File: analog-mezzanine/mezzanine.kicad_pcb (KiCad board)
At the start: 2 copper layers, 90 x 90 mm, 4 parts

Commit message: start layout
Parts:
- added C1: 200n, Capacitor_SMD:C_1206_3216Metric, F.Cu at (149.5, 162.3)
- added C10: 10n, Capacitor_SMD:C_0805_2012Metric, F.Cu at (143.7, 173.0)
- added C11: 10n, Capacitor_SMD:C_0805_2012Metric, F.Cu at (140.7, 173.0)
- added C12: low ESR 2.2u, Capacitor_SMD:C_1206_3216Metric, F.Cu at (132.8, 162.3)
- added C13: 10u alum poly, Capacitor_THT:CP_Radial_D8.0mm_P3.50mm, F.Cu at (127.3, 153.0)
- added C14: 0.1u, Capacitor_SMD:C_1206_3216Metric, F.Cu at (129.4, 162.3)
- added C15: 10u alum poly, Capacitor_THT:CP_Radial_D8.0mm_P3.50mm, F.Cu at (117.8, 153.0)
- added C16: 0.1u, Capacitor_SMD:C_1206_3216Metric, F.Cu at (126.1, 162.3)
- added C17: 0.01u, Capacitor_SMD:C_1206_3216Metric, B.Cu at (38.3, 76.4)
- added C18: 200n, Capacitor_SMD:C_1206_3216Metric, F.Cu at (195.7, 160.3)
- added C19: 200n, Capacitor_SMD:C_1206_3216Metric, F.Cu at (192.4, 160.3)
- added C2: 200n, Capacitor_SMD:C_1206_3216Metric, F.Cu at (146.2, 162.3)
- added C20: 10u alum poly, Capacitor_THT:CP_Radial_D8.0mm_P3.50mm, F.Cu at (192.6, 151.0)
- added C21: 10u alum poly, Capacitor_THT:CP_Radial_D8.0mm_P3.50mm, F.Cu at (183.1, 151.0)
- added C22: low ESR 2.2u, Capacitor_SMD:C_1206_3216Metric, F.Cu at (189.0, 160.3)
- added C23: 10n, Capacitor_SMD:C_0805_2012Metric, F.Cu at (195.9, 171.0)
- added C24: 10n, Capacitor_SMD:C_0805_2012Metric, F.Cu at (192.9, 171.0)
- added C25: low ESR 2.2u, Capacitor_SMD:C_1206_3216Metric, F.Cu at (185.7, 160.3)
- added C26: low ESR 2.2u, Capacitor_SMD:C_1206_3216Metric, F.Cu at (182.3, 160.3)
- added C27: 10n, Capacitor_SMD:C_0805_2012Metric, F.Cu at (189.9, 171.0)
- added C28: 10n, Capacitor_SMD:C_0805_2012Metric, F.Cu at (186.9, 171.0)
- added C29: low ESR 2.2u, Capacitor_SMD:C_1206_3216Metric, F.Cu at (179.0, 160.3)
- added C3: 10u alum poly, Capacitor_THT:CP_Radial_D8.0mm_P3.50mm, F.Cu at (146.4, 153.0)
- added C30: 10u alum poly, Capacitor_THT:CP_Radial_D8.0mm_P3.50mm, F.Cu at (173.5, 151.0)
- added C31: 0.1u, Capacitor_SMD:C_1206_3216Metric, F.Cu at (175.6, 160.3)
- added C32: 10u alum poly, Capacitor_THT:CP_Radial_D8.0mm_P3.50mm, F.Cu at (164.0, 151.0)
- added C33: 0.1u, Capacitor_SMD:C_1206_3216Metric, F.Cu at (172.3, 160.3)
- added C34: 0.01u, Capacitor_SMD:C_1206_3216Metric, B.Cu at (38.3, 84.8)
- added C35: 200n, Capacitor_SMD:C_1206_3216Metric, F.Cu at (131.7, 105.0)
- added C36: 200n, Capacitor_SMD:C_1206_3216Metric, F.Cu at (131.7, 108.3)
- added C37: 10u alum poly, Capacitor_THT:CP_Radial_D8.0mm_P3.50mm, F.Cu at (122.3, 108.1)
- added C38: 10u alum poly, Capacitor_THT:CP_Radial_D8.0mm_P3.50mm, F.Cu at (122.3, 117.6)
- added C39: low ESR 2.2u, Capacitor_SMD:C_1206_3216Metric, F.Cu at (131.7, 111.7)
- added C4: 10u alum poly, Capacitor_THT:CP_Radial_D8.0mm_P3.50mm, F.Cu at (136.9, 153.0)
- added C40: 10n, Capacitor_SMD:C_0805_2012Metric, F.Cu at (142.3, 104.8)
- added C41: 10n, Capacitor_SMD:C_0805_2012Metric, F.Cu at (142.3, 107.8)
- added C42: low ESR 2.2u, Capacitor_SMD:C_1206_3216Metric, F.Cu at (131.7, 115.0)
- added C43: low ESR 2.2u, Capacitor_SMD:C_1206_3216Metric, F.Cu at (131.7, 118.4)
- added C44: 10n, Capacitor_SMD:C_0805_2012Metric, F.Cu at (142.3, 110.8)
- added C45: 10n, Capacitor_SMD:C_0805_2012Metric, F.Cu at (142.3, 113.8)
- added C46: low ESR 2.2u, Capacitor_SMD:C_1206_3216Metric, F.Cu at (131.7, 121.7)
- added C47: 10u alum poly, Capacitor_THT:CP_Radial_D8.0mm_P3.50mm, F.Cu at (122.3, 127.2)
- added C48: 0.1u, Capacitor_SMD:C_1206_3216Metric, F.Cu at (131.7, 125.1)
- added C49: 10u alum poly, Capacitor_THT:CP_Radial_D8.0mm_P3.50mm, F.Cu at (122.3, 136.7)
- added C5: low ESR 2.2u, Capacitor_SMD:C_1206_3216Metric, F.Cu at (142.8, 162.3)
- added C50: 0.1u, Capacitor_SMD:C_1206_3216Metric, F.Cu at (131.7, 128.4)
- added C51: 0.01u, Capacitor_SMD:C_1206_3216Metric, B.Cu at (38.3, 93.2)
- added C52: 200n, Capacitor_SMD:C_1206_3216Metric, F.Cu at (267.5, 159.7)
- added C53: 200n, Capacitor_SMD:C_1206_3216Metric, F.Cu at (264.2, 159.7)
- added C54: 10u alum poly, Capacitor_THT:CP_Radial_D8.0mm_P3.50mm, F.Cu at (264.4, 150.3)
- added C55: 10u alum poly, Capacitor_THT:CP_Radial_D8.0mm_P3.50mm, F.Cu at (254.9, 150.3)
- added C56: low ESR 2.2u, Capacitor_SMD:C_1206_3216Metric, F.Cu at (260.8, 159.7)
- added C57: 10n, Capacitor_SMD:C_0805_2012Metric, F.Cu at (267.7, 170.3)
- added C58: 10n, Capacitor_SMD:C_0805_2012Metric, F.Cu at (264.7, 170.3)
- added C59: low ESR 2.2u, Capacitor_SMD:C_1206_3216Metric, F.Cu at (257.5, 159.7)
- added C6: 10n, Capacitor_SMD:C_0805_2012Metric, F.Cu at (149.7, 173.0)
- added C60: low ESR 2.2u, Capacitor_SMD:C_1206_3216Metric, F.Cu at (254.1, 159.7)
- added C61: 10n, Capacitor_SMD:C_0805_2012Metric, F.Cu at (261.7, 170.3)
- added C62: 10n, Capacitor_SMD:C_0805_2012Metric, F.Cu at (258.7, 170.3)
- added C63: low ESR 2.2u, Capacitor_SMD:C_1206_3216Metric, F.Cu at (250.8, 159.7)
- added C64: 10u alum poly, Capacitor_THT:CP_Radial_D8.0mm_P3.50mm, F.Cu at (245.3, 150.3)
- added C65: 0.1u, Capacitor_SMD:C_1206_3216Metric, F.Cu at (247.4, 159.7)
- added C66: 10u alum poly, Capacitor_THT:CP_Radial_D8.0mm_P3.50mm, F.Cu at (235.8, 150.3)
- added C67: 0.1u, Capacitor_SMD:C_1206_3216Metric, F.Cu at (244.1, 159.7)
- added C68: 0.01u, Capacitor_SMD:C_1206_3216Metric, B.Cu at (38.3, 101.4)
- added C7: 10n, Capacitor_SMD:C_0805_2012Metric, F.Cu at (146.7, 173.0)
- added C8: low ESR 2.2u, Capacitor_SMD:C_1206_3216Metric, F.Cu at (139.5, 162.3)
- added C9: low ESR 2.2u, Capacitor_SMD:C_1206_3216Metric, F.Cu at (136.1, 162.3)
- added FL1: Filter_EMI_LLL, Library:WE-SL3_744252XXX, B.Cu at (57.4, 50.0)
- added FL2: Filter_EMI_LLL, Library:WE-SL3_744252XXX, B.Cu at (71.1, 50.0)
- added FL3: Filter_EMI_LLL, Library:WE-SL3_744252XXX, F.Cu at (58.8, 50.0)
- added FL4: Filter_EMI_LLL, Library:WE-SL3_744252XXX, F.Cu at (69.7, 50.0)
- added J1: Conn_Coaxial, Connector_Coaxial:MMCX_Molex_73415-0961_Horizontal_1.0mm-PCB, F.Cu at (25.1, 76.4)
- added J2: Conn_Coaxial, Connector_Coaxial:MMCX_Molex_73415-0961_Horizontal_1.0mm-PCB, F.Cu at (25.1, 84.9)
- added J3: Conn_Coaxial, Connector_Coaxial:MMCX_Molex_73415-0961_Horizontal_1.0mm-PCB, F.Cu at (25.1, 93.2)
- added J4: Conn_Coaxial, Connector_Coaxial:MMCX_Molex_73415-0961_Horizontal_1.0mm-PCB, F.Cu at (25.1, 101.4)
- added J5: Conn_Coaxial, Connector_Coaxial:MMCX_Molex_73415-1471_Vertical, F.Cu at (46.6, 74.1)
- added J6: Conn_Coaxial, Connector_Coaxial:MMCX_Molex_73415-1471_Vertical, F.Cu at (46.6, 82.5)
- added J7: Conn_Coaxial, Connector_Coaxial:MMCX_Molex_73415-1471_Vertical, F.Cu at (46.6, 90.8)
- added J8: Conn_Coaxial, Connector_Coaxial:MMCX_Molex_73415-1471_Vertical, F.Cu at (46.6, 99.1)
- added J9: LD15P24A4GV00LF, Library:AMPHENOL_LD15P24A4GV00LF, F.Cu at (64.2, 38.4)
- added JP1: SolderJumper_2_Open, Jumper:SolderJumper-2_P1.3mm_Open_RoundedPad1.0x1.5mm, B.Cu at (85.0, 38.4)
- added JP2: SolderJumper_2_Open, Jumper:SolderJumper-2_P1.3mm_Open_RoundedPad1.0x1.5mm, B.Cu at (47.6, 42.4)
- added JP3: SolderJumper_2_Open, Jumper:SolderJumper-2_P1.3mm_Open_RoundedPad1.0x1.5mm, B.Cu at (65.6, 34.5)
- added JP4: SolderJumper_2_Open, Jumper:SolderJumper-2_P1.3mm_Open_RoundedPad1.0x1.5mm, B.Cu at (62.9, 34.5)
- added JP5: SolderJumper_2_Open, Jumper:SolderJumper-2_P1.3mm_Open_RoundedPad1.0x1.5mm, B.Cu at (64.2, 42.4)
- added L1: 33u, Library:IND_VLS4015CX-330M-H, F.Cu at (135.2, 168.4)
- added L2: 33u, Library:IND_VLS4015CX-330M-H, F.Cu at (129.6, 168.4)
- added L3: 33u, Library:IND_VLS4015CX-330M-H, F.Cu at (181.4, 166.4)
- added L4: 33u, Library:IND_VLS4015CX-330M-H, F.Cu at (175.9, 166.4)
- added L5: 33u, Library:IND_VLS4015CX-330M-H, F.Cu at (137.8, 119.3)
- added L6: 33u, Library:IND_VLS4015CX-330M-H, F.Cu at (137.8, 124.9)
- added L7: 33u, Library:IND_VLS4015CX-330M-H, F.Cu at (253.2, 165.8)
- added L8: 33u, Library:IND_VLS4015CX-330M-H, F.Cu at (247.7, 165.8)
- added R1: 1k, Resistor_SMD:R_0805_2012Metric, F.Cu at (34.7, 76.4)
- added R10: 2k, Resistor_SMD:R_0805_2012Metric, F.Cu at (36.5, 86.8)
- added R11: 324k, Resistor_SMD:R_1206_3216Metric, F.Cu at (189.1, 165.9)
- added R12: 100k, Resistor_SMD:R_1206_3216Metric, F.Cu at (185.8, 165.9)
- added R13: 1k, Resistor_SMD:R_0805_2012Metric, F.Cu at (34.7, 93.2)
- added R14: 324k, Resistor_SMD:R_1206_3216Metric, F.Cu at (137.3, 105.0)
- added R15: 100k, Resistor_SMD:R_1206_3216Metric, F.Cu at (137.3, 108.3)
- added R16: 2k, Resistor_SMD:R_0805_2012Metric, F.Cu at (36.5, 95.2)
- added R17: 324k, Resistor_SMD:R_1206_3216Metric, F.Cu at (137.3, 111.6)
- added R18: 100k, Resistor_SMD:R_1206_3216Metric, F.Cu at (137.3, 114.9)
- added R19: 1k, Resistor_SMD:R_0805_2012Metric, F.Cu at (34.7, 101.4)
- added R2: 324k, Resistor_SMD:R_1206_3216Metric, F.Cu at (149.5, 167.9)
- added R20: 324k, Resistor_SMD:R_1206_3216Metric, F.Cu at (267.6, 165.3)
- added R21: 100k, Resistor_SMD:R_1206_3216Metric, F.Cu at (264.3, 165.3)
- added R22: 2k, Resistor_SMD:R_0805_2012Metric, F.Cu at (36.5, 103.4)
- added R23: 324k, Resistor_SMD:R_1206_3216Metric, F.Cu at (260.9, 165.3)
- added R24: 100k, Resistor_SMD:R_1206_3216Metric, F.Cu at (257.6, 165.3)
- added R3: 100k, Resistor_SMD:R_1206_3216Metric, F.Cu at (146.2, 167.9)
- added R4: 2k, Resistor_SMD:R_0805_2012Metric, F.Cu at (36.5, 78.4)
- added R5: 324k, Resistor_SMD:R_1206_3216Metric, F.Cu at (142.9, 167.9)
- added R6: 100k, Resistor_SMD:R_1206_3216Metric, F.Cu at (139.6, 167.9)
- added R7: 1k, Resistor_SMD:R_0805_2012Metric, F.Cu at (34.7, 84.8)
- added R8: 324k, Resistor_SMD:R_1206_3216Metric, F.Cu at (195.8, 165.9)
- added R9: 100k, Resistor_SMD:R_1206_3216Metric, F.Cu at (192.5, 165.9)
- added Rt1: 50, Resistor_SMD:R_0805_2012Metric, F.Cu at (31.2, 75.5)
- added Rt2: 50, Resistor_SMD:R_0805_2012Metric, F.Cu at (42.4, 74.1)
- added Rt3: 50, Resistor_SMD:R_0805_2012Metric, F.Cu at (31.2, 83.9)
- added Rt4: 50, Resistor_SMD:R_0805_2012Metric, F.Cu at (42.4, 82.6)
- added Rt5: 50, Resistor_SMD:R_0805_2012Metric, F.Cu at (31.2, 92.3)
- added Rt6: 50, Resistor_SMD:R_0805_2012Metric, F.Cu at (42.4, 90.9)
- added Rt7: 50, Resistor_SMD:R_0805_2012Metric, F.Cu at (31.2, 100.5)
- added Rt8: 50, Resistor_SMD:R_0805_2012Metric, F.Cu at (42.4, 99.1)
- added U1: minus TPS7A3001MDGNTEP, Library:DGN8_1P89X1P57, F.Cu at (117.5, 163.2)
- added U10: minus TPS7A3001MDGNTEP, Library:DGN8_1P89X1P57, F.Cu at (235.5, 160.5)
- added U11: plus TPS7A4901DGNT, Library:SOP65P490X110-9N, F.Cu at (240.1, 161.1)
- added U12: BUF602xDBV, Package_TO_SOT_SMD:SOT-23-5, F.Cu at (38.8, 100.3)
- added U2: plus TPS7A4901DGNT, Library:SOP65P490X110-9N, F.Cu at (122.1, 163.8)
- added U3: BUF602xDBV, Package_TO_SOT_SMD:SOT-23-5, F.Cu at (38.8, 75.3)
- added U4: minus TPS7A3001MDGNTEP, Library:DGN8_1P89X1P57, F.Cu at (163.7, 161.2)
- added U5: plus TPS7A4901DGNT, Library:SOP65P490X110-9N, F.Cu at (168.3, 161.8)
- added U6: BUF602xDBV, Package_TO_SOT_SMD:SOT-23-5, F.Cu at (38.8, 83.7)
- added U7: minus TPS7A3001MDGNTEP, Library:DGN8_1P89X1P57, F.Cu at (132.6, 137.0)
- added U8: plus TPS7A4901DGNT, Library:SOP65P490X110-9N, F.Cu at (133.2, 132.4)
- added U9: BUF602xDBV, Package_TO_SOT_SMD:SOT-23-5, F.Cu at (38.8, 92.1)
- moved H2 171.3 mm to (28.9, 29.3), turned to 180 degrees
- moved H4 155.4 mm to (26.4, 109.3), turned to 180 degrees
- moved H3 101.3 mm to (103.9, 29.3), turned to 180 degrees
- moved H1 61.5 mm to (106.4, 109.3), turned to 180 degrees
- renumbered H3 to H2, H2 to H3
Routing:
- net Net-(FL2-5): track 0.00 -> 9.65 mm
- net Net-(FL2-1): track 0.00 -> 9.65 mm
- net Net-(FL1-5): track 0.00 -> 9.65 mm
- net Net-(FL1-1): track 0.00 -> 9.65 mm
- net Net-(FL2-3): track 0.00 -> 9.57 mm
- net Net-(FL1-3): track 0.00 -> 9.57 mm
- net Net-(FL4-5): track 0.00 -> 6.81 mm
- net Net-(FL4-1): track 0.00 -> 6.81 mm
- net Net-(FL3-5): track 0.00 -> 6.81 mm
- net Net-(FL3-1): track 0.00 -> 6.81 mm
- net Net-(FL4-3): track 0.00 -> 6.73 mm
- net Net-(FL3-3): track 0.00 -> 6.73 mm
- net Net-(U4-OUT): track 0.00 -> 4.14 mm, vias 0 -> 1
- net Net-(U1-OUT): track 0.00 -> 4.14 mm, vias 0 -> 1
- net Net-(U7-OUT): track 0.00 -> 4.14 mm, vias 0 -> 1
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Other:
- outline, holes or cut-outs redrawn

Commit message: laid out chunks and power
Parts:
- C11, C12, C14, C16, C19, C2, C23, C25, C28, C29, C31, C33, C36, C40, C42, C45, C46, C48, C50, C53, C57, C59, C6, C62, C63, C65, C67, C8, L2, L4, L6, L8, R11, R12, R17, R18, R23, R24, R5, R6, U11, U2, U5, U8: moved to B.Cu
- C13, C20, C3, C30, C37, C47, C54, C64: value 10u alum poly -> low ESR 10u; footprint Capacitor_THT:CP_Radial_D8.0mm_P3.50mm -> Capacitor_SMD:C_1206_3216Metric
- C15, C21, C32, C38, C4, C49, C55, C66: value 10u alum poly -> low ESR 10u; footprint Capacitor_THT:CP_Radial_D8.0mm_P3.50mm -> Capacitor_SMD:C_1206_3216Metric; moved to B.Cu
- J1, J2, J3, J4: footprint Connector_Coaxial:MMCX_Molex_73415-0961_Horizontal_1.0mm-PCB -> Connector_Coaxial:MMCX_Molex_73415-1471_Vertical
- moved C62 263.4 mm to (31.4, 37.1), turned to 90 degrees
- moved R23 260.9 mm to (33.7, 37.1), turned to 90 degrees
- moved C58 260.8 mm to (42.3, 34.0), turned to 90 degrees
- moved R24 260.3 mm to (33.7, 32.4), turned to 90 degrees
- moved R20 259.5 mm to (34.7, 50.9)
- moved C61 258.5 mm to (32.4, 50.9)
- moved R21 254.5 mm to (34.7, 55.6)
- moved C57 254.4 mm to (41.5, 54.0)
- moved C59 247.2 mm to (41.3, 39.7), turned to 90 degrees
- moved C53 246.7 mm to (50.2, 36.7)
- moved C63 245.2 mm to (37.6, 38.5), turned to 180 degrees
- moved C56 245.1 mm to (42.5, 48.4)
- moved C67 242.9 mm to (31.0, 43.0), turned to 0 degrees
- moved C60 241.9 mm to (38.8, 49.5), turned to 180 degrees
- moved C52 241.2 mm to (50.7, 54.2)
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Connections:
- C15 pad 1: Net-(U2-OUT) -> GND
- C15 pad 2: GND -> Net-(U2-OUT)
- C21 pad 1: Net-(U5-EN) -> GND
- C21 pad 2: GND -> Net-(U5-EN)
- C32 pad 1: Net-(U5-OUT) -> GND
- C32 pad 2: GND -> Net-(U5-OUT)
- C38 pad 1: Net-(U8-EN) -> GND
- C38 pad 2: GND -> Net-(U8-EN)
- C4 pad 1: Net-(U2-EN) -> GND
- C4 pad 2: GND -> Net-(U2-EN)
- C49 pad 1: Net-(U8-OUT) -> GND
- C49 pad 2: GND -> Net-(U8-OUT)
- C55 pad 1: Net-(U11-EN) -> GND
- C55 pad 2: GND -> Net-(U11-EN)
- C66 pad 1: Net-(U11-OUT) -> GND
- C66 pad 2: GND -> Net-(U11-OUT)
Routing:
- net GND: track 0.00 -> 72.5 mm
- net /+7D: track 0.00 -> 63.1 mm, vias 0 -> 1
- net /-7C: track 0.00 -> 56.8 mm
- net /+7C: track 0.00 -> 40.5 mm, vias 0 -> 1
- net /-7D: track 0.00 -> 40.2 mm
- net /+7B: track 0.00 -> 28.4 mm
- net /-7A: track 0.00 -> 23.6 mm, vias 0 -> 1
- net /-7B: track 0.00 -> 11.2 mm, vias 0 -> 1
- net /+7A: track 0.00 -> 9.49 mm
- net Net-(U8-NR/SS): track 0.00 -> 1.95 mm, vias 0 -> 1
- net Net-(U5-NR/SS): track 0.00 -> 1.95 mm, vias 0 -> 1
- net Net-(U2-NR/SS): track 0.00 -> 1.95 mm, vias 0 -> 1
- net Net-(U11-NR/SS): track 0.00 -> 1.95 mm, vias 0 -> 1
- net Net-(U7-NR/SS): vias 0 -> 1
- net Net-(U4-NR/SS): vias 0 -> 1
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- added copper zone on B.Cu, net GND
- added copper zone on F.Cu, net GND
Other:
- outline, holes or cut-outs redrawn

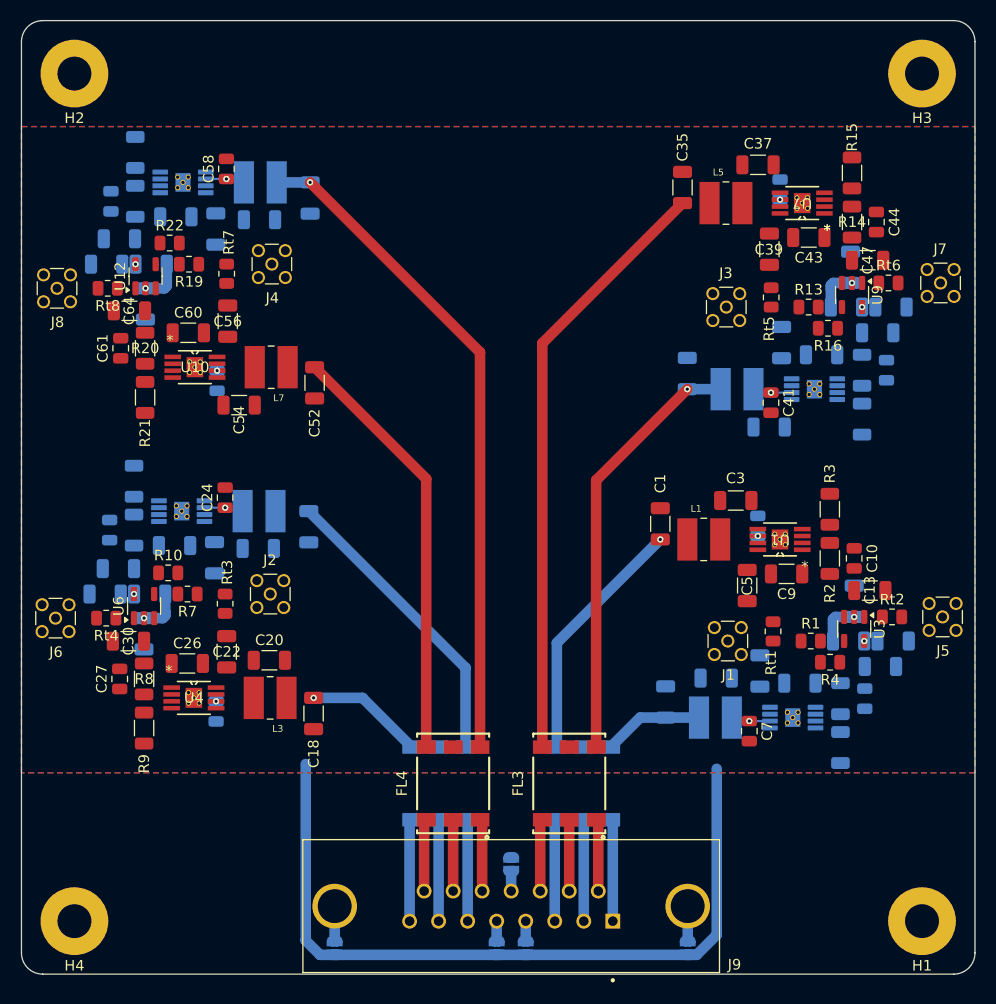
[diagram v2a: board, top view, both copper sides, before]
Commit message: re-layout, better ground plane config
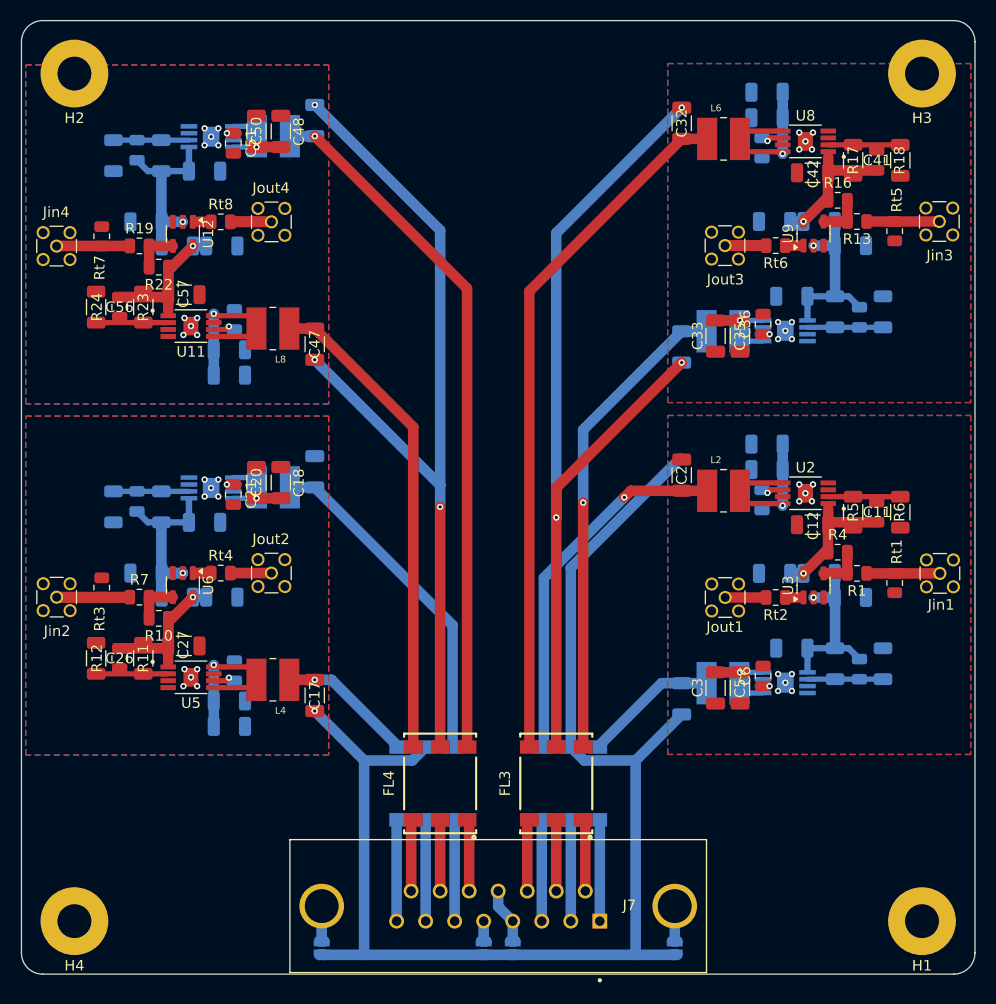
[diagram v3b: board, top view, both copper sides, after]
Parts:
- removed the C13 at (103.1, 73.8)
- removed the C15 at (104.1, 81.0)
- removed the C30 at (33.1, 78.6)
- removed the C32 at (32.1, 71.7)
- removed the C47 at (102.9, 42.6)
- removed the C49 at (103.8, 49.5)
- removed C64, C66: low ESR 10u, Capacitor_SMD:C_1206_3216Metric
- removed JP5: SolderJumper_2_Open, Jumper:SolderJumper-2_P1.3mm_Open_RoundedPad1.0x1.5mm
- C1, C10, C7, C9, L1, L3, L5, L7, R14, R15, R2, R20, R21, R3, R8, R9, U1, U10, U4, U7: moved to B.Cu
- C11, C12, C2, C6, L2, L4, L6, L8, R11, R12, R17, R18, R23, R24, R5, R6, U11, U2, U5, U8: moved to F.Cu
- C16: renamed from C18; moved to B.Cu
- C17: renamed from C19; moved to F.Cu
- C21: renamed from C23; moved to F.Cu
- C22: renamed from C24; moved to B.Cu
- C24: renamed from C26; moved to B.Cu
- C25: renamed from C27; moved to B.Cu
- C26: renamed from C28; moved to F.Cu
- C27: renamed from C29; moved to F.Cu
- C31: renamed from C35; moved to B.Cu
- C32: renamed from C36; moved to F.Cu
- C36: renamed from C40; moved to F.Cu
- C37: renamed from C41; moved to B.Cu
- C39: renamed from C43; moved to B.Cu
- C40: renamed from C44; moved to B.Cu
- C41: renamed from C45; moved to F.Cu
- C42: renamed from C46; moved to F.Cu
- C46: renamed from C52; moved to B.Cu
- C47: renamed from C53; moved to F.Cu
- C51: renamed from C57; moved to F.Cu
- C52: renamed from C58; moved to B.Cu
- C54: renamed from C60; moved to B.Cu
- C55: renamed from C61; moved to B.Cu
- C56: renamed from C62; moved to F.Cu
- C57: renamed from C63; moved to F.Cu
- moved C34 31.6 mm to (93.4, 26.8), turned to 0 degrees
- moved C48 26.1 mm to (47.5, 30.5), turned to -90 degrees
- moved C46 24.8 mm to (50.7, 29.4), turned to 90 degrees
- moved R18 24.7 mm to (106.0, 33.2)
- moved C37 24.1 mm to (92.9, 32.0)
- moved L6 23.7 mm to (89.3, 31.2)
- moved C32 23.6 mm to (85.3, 29.7)
- moved U8 23.4 mm to (97.0, 31.4)
- moved R21 23.0 mm to (31.7, 32.7)
- moved R6 22.9 mm to (106.0, 66.4)
- moved C16 22.8 mm to (50.7, 62.6), turned to 90 degrees
- moved C4 22.6 mm to (93.4, 60.0)
- moved C51 22.5 mm to (43.0, 31.6)
- moved C7 21.9 mm to (92.9, 65.2)
- moved U10 21.8 mm to (40.9, 31.0)
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- renumbered C14 to C13, C16 to C14, C17 to C15, C20 to C18, C21 to C19, C22 to C20, C25 to C23, C31 to C28, C33 to C29, C34 to C30, C37 to C33, C38 to C34, C39 to C35, C42 to C38, C48 to C43, C50 to C44, C51 to C45, C54 to C48, C55 to C49, C56 to C50, C59 to C53, C65 to C58, C67 to C59, C68 to C60, J9 to J7, J1 to Jin1, J2 to Jin2, J3 to Jin3, J4 to Jin4, J5 to Jout1, J6 to Jout2, J7 to Jout3, J8 to Jout4
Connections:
- FL1 pad 4: /+7A -> /-7A
- FL1 pad 6: /-7A -> /+7A
- FL2 pad 4: /+7B -> /-7B
- FL2 pad 6: /-7B -> /+7B
- FL3 pad 4: /-7C -> /+7C
- FL3 pad 6: /+7C -> /-7C
- FL4 pad 4: /-7D -> /+7D
- FL4 pad 6: /+7D -> /-7D
- J7 pad 12: Net-(JP5-B) -> Net-(JP4-B)
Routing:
- net GND: track 72.5 -> 294.4 mm, vias 0 -> 47
- net /-7D: track 40.2 -> 66.0 mm, vias 0 -> 1
- net /+7A: track 9.49 -> 34.8 mm, vias 0 -> 1
- net /+7C: track 40.5 -> 65.8 mm, vias 1 -> 0
- net /-7B: track 11.2 -> 32.2 mm, vias 1 -> 0
- net Net-(U4-OUT): track 4.14 -> 22.2 mm
- net /+7D: track 63.1 -> 45.8 mm, vias 1 -> 0
- net /+7B: track 28.4 -> 13.0 mm, vias 0 -> 1
- net Net-(U2-EN): track 0.00 -> 14.5 mm, vias 0 -> 1
- net Net-(U8-EN): track 0.00 -> 14.5 mm, vias 0 -> 1
- net Net-(U5-EN): track 0.00 -> 14.5 mm, vias 0 -> 1
- net Net-(U11-EN): track 0.00 -> 14.5 mm, vias 0 -> 1
- net Net-(U7-OUT): track 4.14 -> 18.1 mm
- net Net-(U10-OUT): track 4.14 -> 18.1 mm
- net /offset module1/preamp in: track 0.00 -> 13.8 mm
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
